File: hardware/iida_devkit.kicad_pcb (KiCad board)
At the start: 4 copper layers, 178.2 x 77.6 mm, 224 parts, among them J1001 132134, J201 USB4105-GF-A, J202 PRPC001DAAN-RC, J301 B2B-XH-A, J302 PRPC001DAAN-RC, J401 61300111121, J402 61300111121, J403 PRPC001DAAN-RC, J404 61300111121, J405 PRPC001DAAN-RC, J406 PRPC001DAAN-RC, J407 61300111121, J501 PRPC006SAAN-RC, J502 TC2050, J503 61300611121, J504 61300611121, J505 61300611121, J506 61300611121, J507 61300611121, J508 PRPC001DAAN-RC, J509 PRPC006SAAN-RC, J901 SIM8066-6-1-14-01-A, Q301 IRLML6401TRPBF, Q302 DMN2005, Q303 DMN2005, Q501 BSS806NH, Q801 BSS806NH, Q802 IRLML6401TRPBF, Q803 BSS806NH, Q804 BSS806NH, Q805 BSS806NH, U301 BQ29728DSER, U302 MCP73833T-FCI/MF, U303 MAX17048G+T10, U401 LM66200DRLR, U402 TPS63020DSJR, U403 LD39200DPUR, U501 STM32L552CEU6, U502 AT25SF081B-MAHB-T, U601 MCP9808T-E/MC, U602 SHT40-AD1B-R2, U701 TCA9554PW, U801 SN74AVC4T774, U802 SARA-R500S-01B, Y501 ECS-160-9-37-CKM-TR3, Y502 ABS05-32.768KHZ-9-T

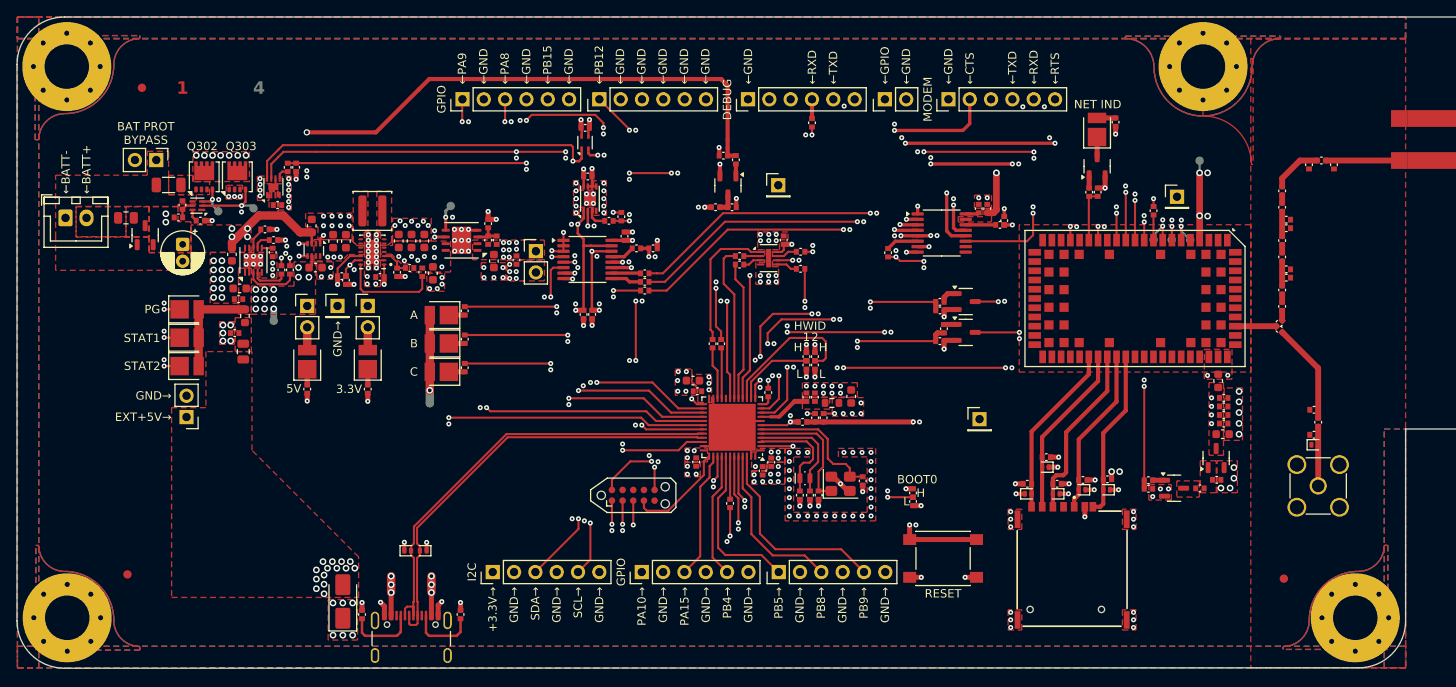
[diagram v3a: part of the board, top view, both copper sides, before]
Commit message: HW: Fix impedance controlled traces
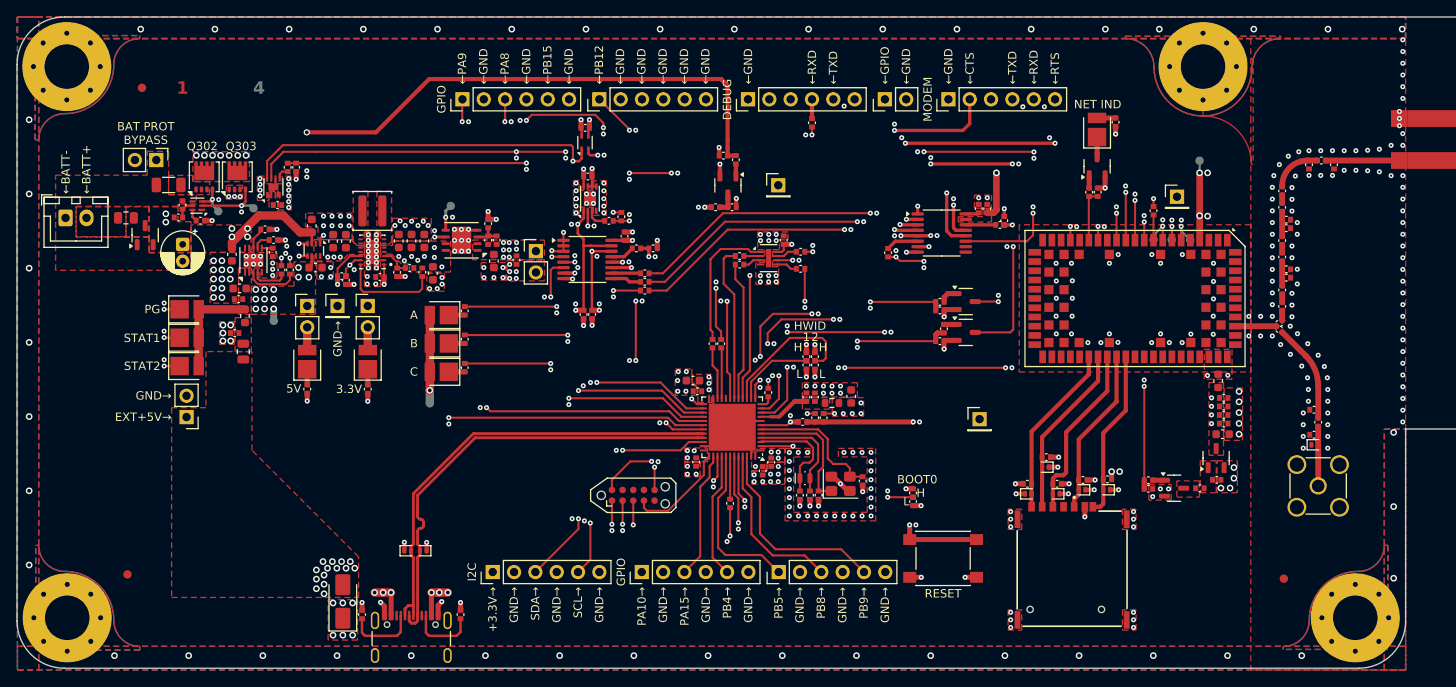
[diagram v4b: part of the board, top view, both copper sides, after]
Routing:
- net /Modem/PWR_ON: track 33.1 -> 25.5 mm
- net /Microcontroller/USB_DP: track 52.4 -> 54.7 mm
- net /Microcontroller/USB_DN: track 53.0 -> 54.2 mm
- net /Microcontroller/GPIO_PA10: track 25.1 -> 24.3 mm
- net GND: vias 368 -> 546
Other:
- outline, holes or cut-outs redrawn

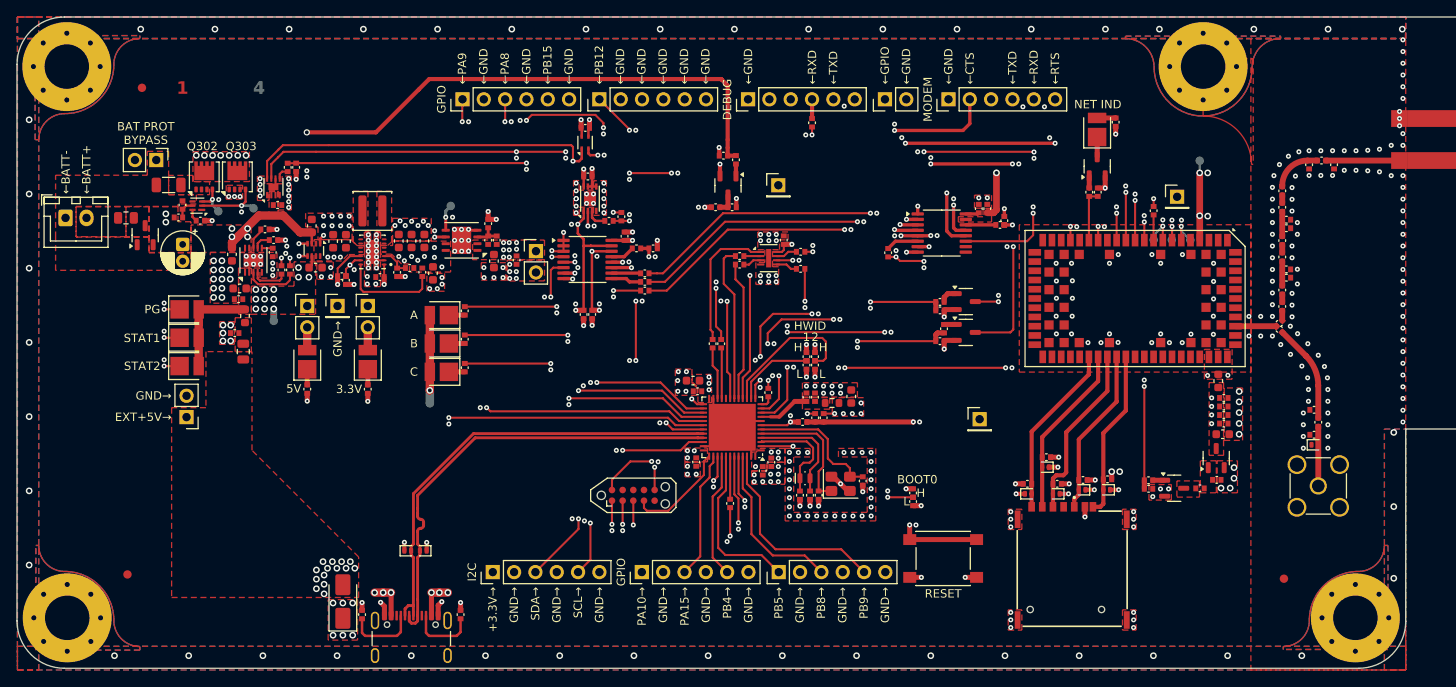
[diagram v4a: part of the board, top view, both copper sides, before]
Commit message: HW: Add power fills
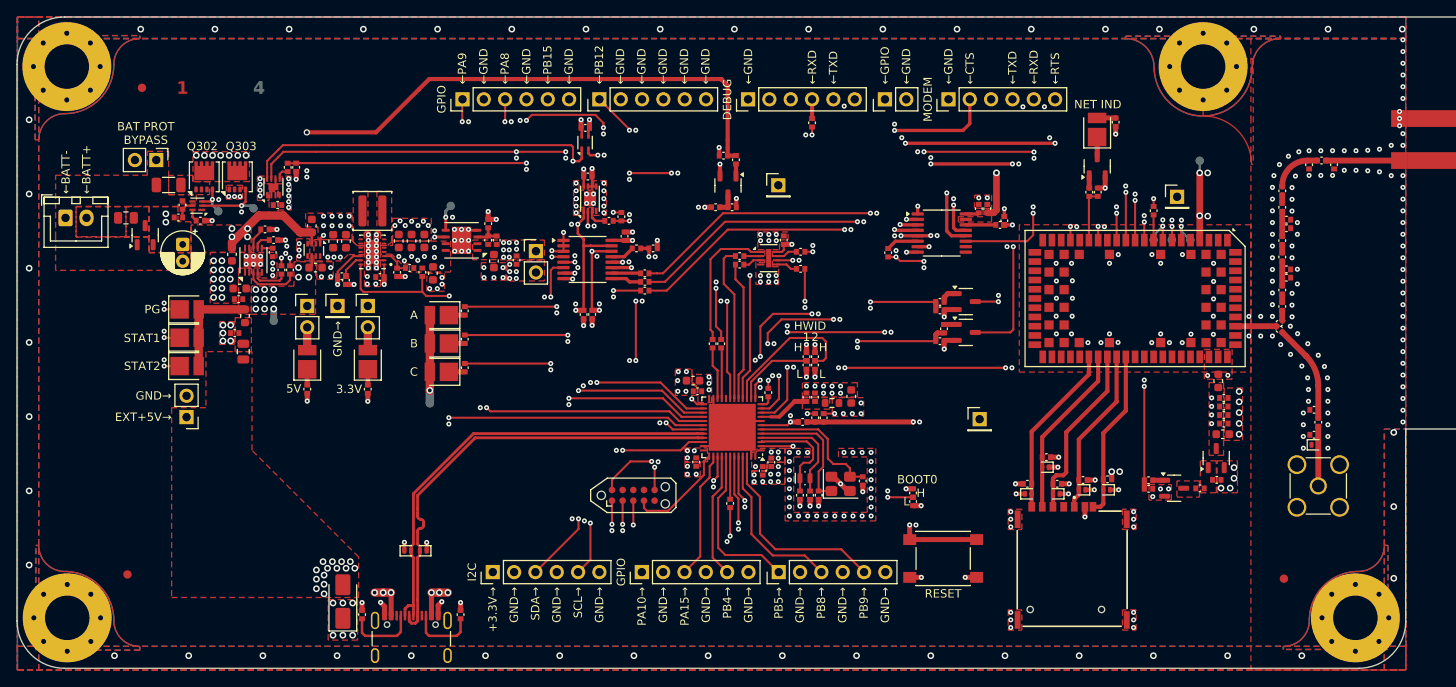
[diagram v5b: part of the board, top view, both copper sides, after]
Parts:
- renumbered TP402 to TP401, TP403 to TP402, TP404 to TP403
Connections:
- C410 pad 1: /Power/V_SYS -> /Power/V_3V3_OUT
- C411 pad 1: /Power/V_SYS -> /Power/V_3V3_OUT
- J405 pad 1: /Power/V_SYS -> /Power/V_3V3_OUT
- R406 pad 1: /Power/V_SYS -> /Power/V_3V3_OUT
- R409 pad 2: /Power/V_SYS -> /Power/V_3V3_OUT
- U403 pad 1: /Power/V_SYS -> /Power/V_3V3_OUT
- U403 pad 2: /Power/V_SYS -> /Power/V_3V3_OUT
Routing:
- net /Power/V_3V3_EN: track 13.3 -> 25.6 mm, vias 1 -> 2
- net GND: track 88.2 -> 86.2 mm
- net /Power/PS/SYNC: track 3.01 -> 2.93 mm, vias 1 -> 0
- net /Power/V_SYS: vias 11 -> 3
- net /Power/V_3V3_OUT: vias 0 -> 8
- added copper zone on F.Cu, net /Power/V_3V3_OUT
- added copper zone on In2.Cu, net /Power/V_3V3_OUT
